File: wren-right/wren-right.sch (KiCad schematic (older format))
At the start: 61 parts, among them J1 TRRS_Jack, SW0 Reset, U1 ProMicro

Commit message: Switch to Elite C Footprints
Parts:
- U1: value ProMicro -> Elite C; footprint footprints:ARDUINO_PRO_MICRO -> footprints:Elite-C; symbol random-keyboard-parts:ProMicro_2 -> keebio:Elite-C
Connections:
- no-connect marks 5 -> 11
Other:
- moved on the sheet: SW0
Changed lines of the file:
@@
 	1    0    0    -1
 $EndComp
-Text GLabel 1950 3050 0    50   BiDi ~ 0
+Text GLabel 1050 1450 0    50   BiDi ~ 0
 SDA
-Text GLabel 1950 3150 0    50   BiDi ~ 0
+Text GLabel 1050 1550 0    50   BiDi ~ 0
 SCL
-Text GLabel 3250 2950 2    50   Output ~ 0
+Text GLabel 2450 1350 2    50   Output ~ 0
 VCC
 Text GLabel 3950 4550 2    50   Input ~ 0
@@
 Text GLabel 2850 4550 2    50   Output ~ 0
 GND
-Text GLabel 3250 2750 2    50   Input ~ 0
+Text GLabel 2450 1150 2    50   Input ~ 0
 GND
 $Comp
@@
 L Switch:SW_Push SW0
 U 1 1 60738E12
-P 3750 2850
-F 0 "SW0" H 3750 3135 50  0000 C CNN
-F 1 "Reset" H 3750 3044 50  0000 C CNN
-F 2 "Button_Switch_THT:SW_PUSH_6mm" H 3750 3050 50  0001 C CNN
-F 3 "~" H 3750 3050 50  0001 C CNN
-	1    3750 2850
-	1    0    0    -1
-$EndComp
-Wire Wire Line
-	3250 2850 3550 2850
-Text GLabel 3950 2850 2    50   Output ~ 0
+P 2950 1250
+F 0 "SW0" H 2950 1535 50  0000 C CNN
+F 1 "Reset" H 2950 1444 50  0000 C CNN
+F 2 "Button_Switch_THT:SW_PUSH_6mm" H 2950 1450 50  0001 C CNN
+F 3 "~" H 2950 1450 50  0001 C CNN
+	1    2950 1250
+	1    0    0    -1
+$EndComp
+Wire Wire Line
+	2450 1250 2750 1250
+Text GLabel 3150 1250 2    50   Output ~ 0
 GND
 $Comp
@@
 Text GLabel 7750 2350 1    50   Input ~ 0
 COL5
-Text GLabel 1950 3250 0    50   Input ~ 0
+Text GLabel 1050 1650 0    50   Input ~ 0
 COL0
-Text GLabel 1950 3350 0    50   Input ~ 0
+Text GLabel 1050 1750 0    50   Input ~ 0
 COL1
-Text GLabel 1950 3450 0    50   Input ~ 0
+Text GLabel 1050 1850 0    50   Input ~ 0
 COL2
-Text GLabel 1950 3550 0    50   Input ~ 0
+Text GLabel 1050 1950 0    50   Input ~ 0
 COL3
-Text GLabel 1950 3650 0    50   Input ~ 0
+Text GLabel 1050 2050 0    50   Input ~ 0
 COL4
-Text GLabel 3250 3550 2    50   Input ~ 0
+Text GLabel 2450 1950 2    50   Input ~ 0
 ROW2
-Text GLabel 3250 3650 2    50   Input ~ 0
+Text GLabel 2450 2050 2    50   Input ~ 0
 ROW3
-Text GLabel 3250 3750 2    50   Input ~ 0
+Text GLabel 2450 2150 2    50   Input ~ 0
 ROW4
 $Comp
@@
 Text GLabel 3950 4250 2    50   BiDi ~ 0
 SDA
-Text GLabel 3250 3450 2    50   Input ~ 0
+Text GLabel 2450 1850 2    50   Input ~ 0
 ROW1
-Text GLabel 3250 3350 2    50   Input ~ 0
+Text GLabel 2450 1750 2    50   Input ~ 0
 ROW0
-NoConn ~ 3250 3150
-NoConn ~ 3250 3050
-Text GLabel 1950 3750 0    50   Input ~ 0
+NoConn ~ 2450 1550
+NoConn ~ 2450 1450
+Text GLabel 1050 2150 0    50   Input ~ 0
 COL5
-NoConn ~ 3250 3250
-$Comp
-L random-keyboard-parts:ProMicro_2 U1
+NoConn ~ 2450 1650
+$Comp
+L keebio:Elite-C U1
 U 1 1 6071F7CA
-P 2600 3200
-F 0 "U1" H 2600 4015 50  0000 C CNN
-F 1 "ProMicro" H 2600 3924 50  0000 C CNN
-F 2 "footprints:ARDUINO_PRO_MICRO" H 2550 3300 50  0001 C CNN
-F 3 "" H 2550 3300 50  0001 C CNN
-	1    2600 3200
+P 1750 1600
+F 0 "U1" H 1750 2415 50  0000 C CNN
+F 1 "Elite C" H 1750 2324 50  0000 C CNN
+F 2 "footprints:Elite-C" H 1700 1700 50  0001 C CNN
+F 3 "" H 1700 1700 50  0001 C CNN
+	1    1750 1600
 	1    0    0    -1
 $EndComp
@@
 Wire Wire Line
 	7350 2900 7550 2900
-NoConn ~ 1950 2650
-NoConn ~ 1950 2750
+NoConn ~ 1050 1050
+NoConn ~ 1050 1150
+Text GLabel 850  1250 2    50   Output ~ 0
+GND
+Text GLabel 850  1350 2    50   Output ~ 0
+GND
+NoConn ~ 1550 2550
+NoConn ~ 1650 2550
+NoConn ~ 1750 2550
+NoConn ~ 1850 2550
+NoConn ~ 1950 2550
+NoConn ~ 2450 1050
 $EndSCHEMATC

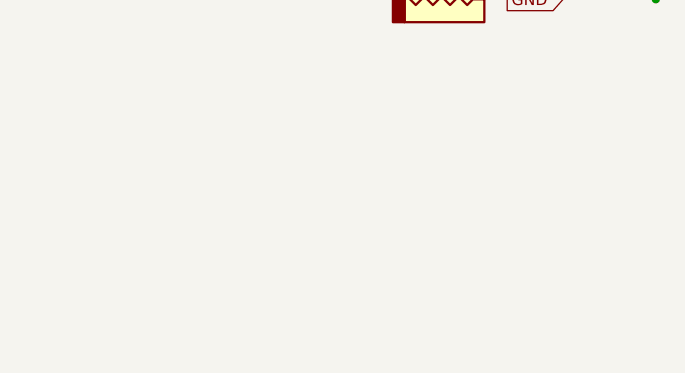
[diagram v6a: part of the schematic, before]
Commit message: Add Encoders to PCB
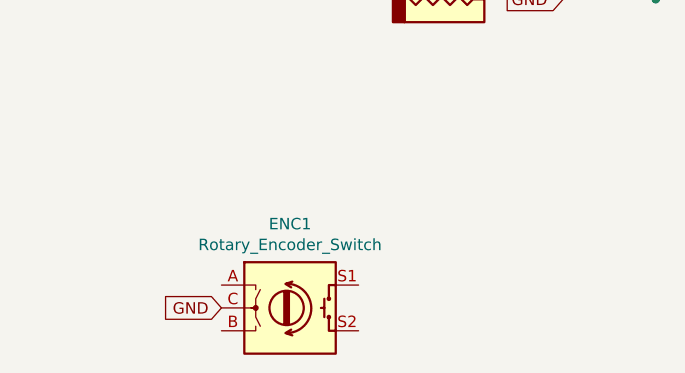
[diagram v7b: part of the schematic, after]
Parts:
- added ENC1: Rotary_Encoder_Switch, Rotary_Encoder:RotaryEncoder_Alps_EC11E-Switch_Vertical_H20mm, symbol Device:Rotary_Encoder_Switch
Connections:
- net GND: now also ENC1.C
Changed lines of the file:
@@
 NoConn ~ 1950 2550
 NoConn ~ 2450 1050
+$Comp
+L Device:Rotary_Encoder_Switch ENC1
+U 1 1 6077ECF3
+P 1900 5900
+F 0 "ENC1" H 1900 6267 50  0000 C CNN
+F 1 "Rotary_Encoder_Switch" H 1900 6176 50  0000 C CNN
+F 2 "Rotary_Encoder:RotaryEncoder_Alps_EC11E-Switch_Vertical_H20mm" H 1750 6060 50  0001 C CNN
+F 3 "~" H 1900 6160 50  0001 C CNN
+	1    1900 5900
+	1    0    0    -1
+$EndComp
+Text GLabel 1600 5900 0    50   Input ~ 0
+GND
 $EndSCHEMATC

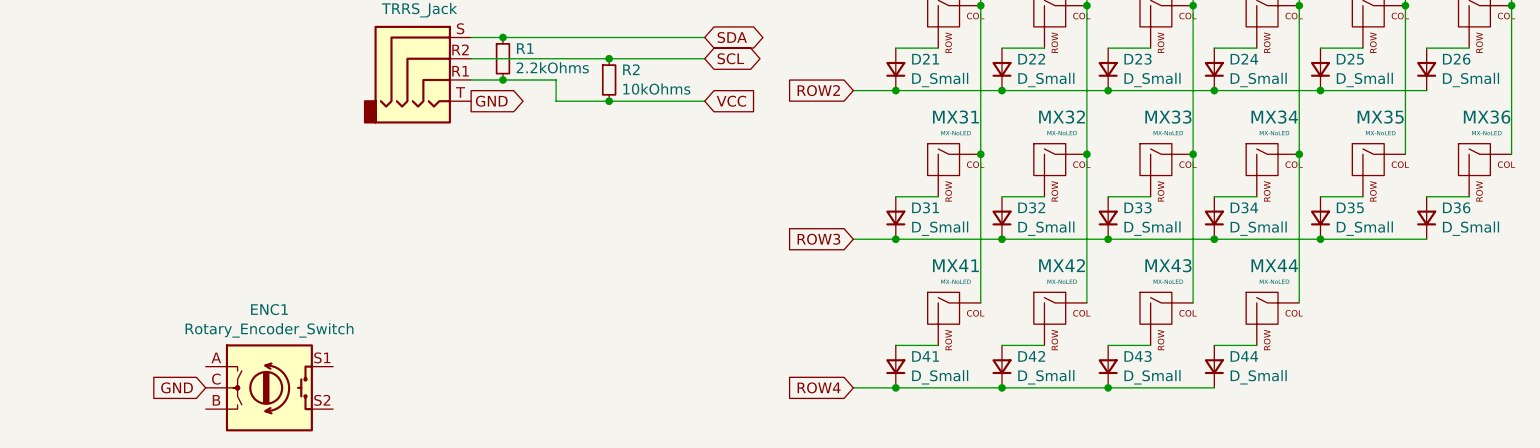
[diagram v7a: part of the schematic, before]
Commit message: Component Updates
Switch to through-hole diodes and resistors, reroute traces, etc.
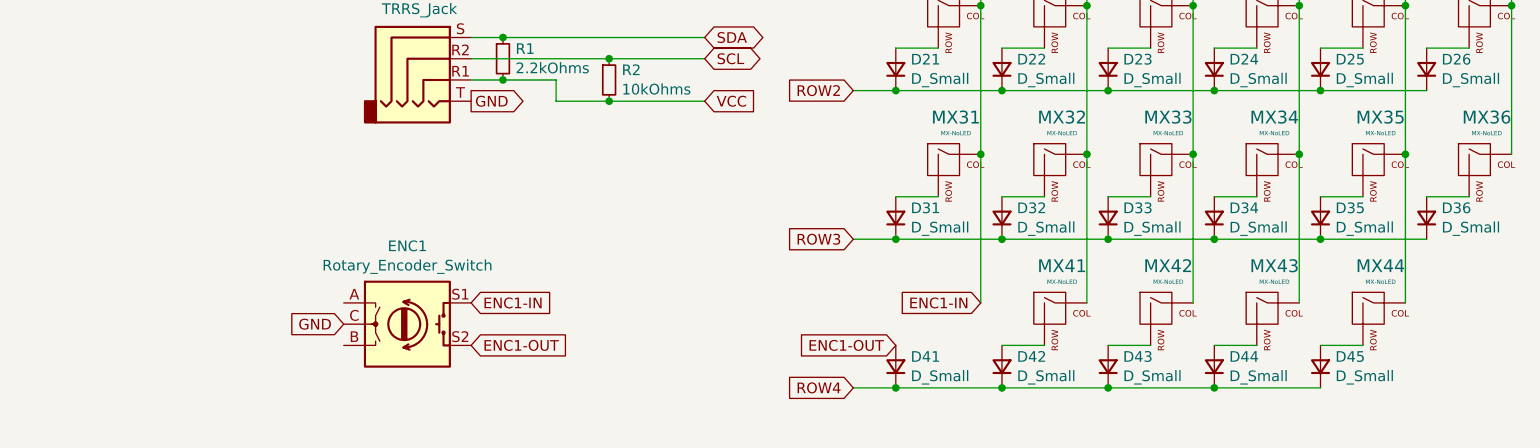
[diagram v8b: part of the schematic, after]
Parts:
- added D41: D_Small, footprints:D_SOD123_axial, symbol Device:D_Small
- D1, D11, D12, D13, D14, D15, D16, D2, D21, D22, D23, D24, D25, D26, D3, D31, D32, D33, D34, D35, D36, D4, D5, D6: footprint Diode_SMD:D_SOD-123 -> footprints:D_SOD123_axial
- D42: renamed from D41; footprint Diode_SMD:D_SOD-123 -> footprints:D_SOD123_axial
- D43: renamed from D42; footprint Diode_SMD:D_SOD-123 -> footprints:D_SOD123_axial
- D44: renamed from D43; footprint Diode_SMD:D_SOD-123 -> footprints:D_SOD123_axial
- D45: renamed from D44; footprint Diode_SMD:D_SOD-123 -> footprints:D_SOD123_axial
- R1, R2: footprint Resistor_SMD:R_0805_2012Metric -> Resistor_THT:R_Axial_DIN0204_L3.6mm_D1.6mm_P5.08mm_Vertical
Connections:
- net COL0: now also ENC1.S1; no longer MX41.1 (COL)
- net COL1: now also MX41.1 (COL); no longer MX42.1 (COL)
- net COL2: now also MX42.1 (COL); no longer MX43.1 (COL)
- net COL3: now also MX43.1 (COL); no longer MX44.1 (COL)
- net COL4: now also MX44.1 (COL)
- net ROW4: now also D41.1 (K)
- net ENC1-OUT: now reaches ENC1.S2
- net ENC1-OUT: now also D41.2 (A)
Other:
- moved on the sheet: D42, D43, D44, D45, ENC1, MX41, MX42, MX43, MX44
